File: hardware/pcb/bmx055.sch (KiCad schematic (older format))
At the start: 1 part, among them U3 BMX055

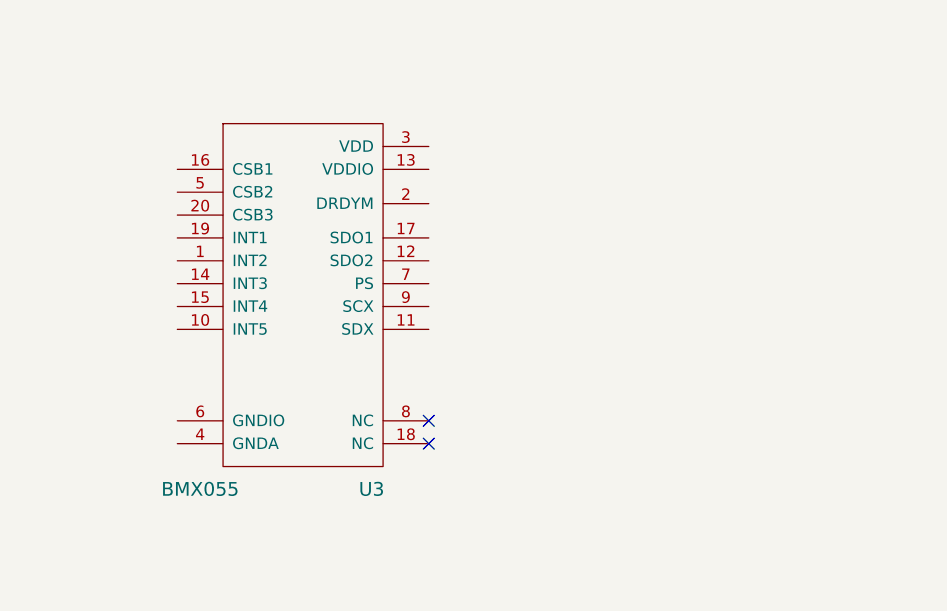
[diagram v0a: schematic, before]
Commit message: Added mcu, connected nrf8001 and flash, new footprint, other changes
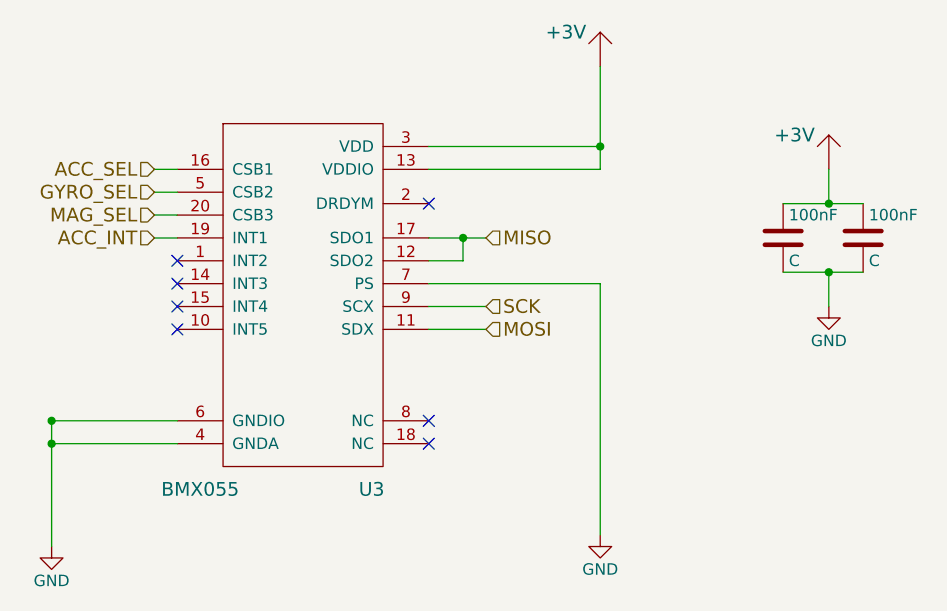
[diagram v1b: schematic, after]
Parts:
- added 100nF (x2): C, symbol C
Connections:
- net MOSI: now reaches U3.11 (SDX)
- net MISO: now reaches U3.12 (SDO2)
- net MISO: now also U3.17 (SDO1)
- net +3V3: now reaches U3.13 (VDDIO)
- net +3V3: now also U3.3 (VDD), 100nF.1, 100nF.1
- net ACC_SEL: now reaches U3.16 (CSB1)
- net ACC_INT: now reaches U3.19 (INT1)
- net MAG_SEL: now reaches U3.20 (CSB3)
- net GND: now reaches U3.4 (GNDA)
- net GND: now also U3.6 (GNDIO), U3.7 (PS), 100nF.2, 100nF.2
- net GYRO_SEL: now reaches U3.5 (CSB2)
- net SCK: now reaches U3.9 (SCX)
- no-connect marks 2 -> 7
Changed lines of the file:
@@
 $Descr A4 11693 8268
 encoding utf-8
-Sheet 4 4
+Sheet 4 5
 Title ""
 Date ""
@@
 NoConn ~ 6150 3650
 NoConn ~ 6150 3550
+$Comp
+L +3V #PWR?
+U 1 1 552EACA4
+P 6900 2000
+F 0 "#PWR?" H 6900 1900 60  0001 C CNN
+F 1 "+3V" H 6750 2150 60  0000 C CNN
+F 2 "" H 6900 2000 60  0000 C CNN
+F 3 "" H 6900 2000 60  0000 C CNN
+	1    6900 2000
+	1    0    0    -1
+$EndComp
+$Comp
+L GND #PWR?
+U 1 1 552EACBF
+P 6900 4050
+F 0 "#PWR?" H 6900 3800 50  0001 C CNN
+F 1 "GND" H 6900 3900 50  0000 C CNN
+F 2 "" H 6900 4050 60  0000 C CNN
+F 3 "" H 6900 4050 60  0000 C CNN
+	1    6900 4050
+	1    0    0    -1
+$EndComp
+$Comp
+L GND #PWR?
+U 1 1 552EACD5
+P 4500 4100
+F 0 "#PWR?" H 4500 3850 50  0001 C CNN
+F 1 "GND" H 4500 3950 50  0000 C CNN
+F 2 "" H 4500 4100 60  0000 C CNN
+F 3 "" H 4500 4100 60  0000 C CNN
+	1    4500 4100
+	1    0    0    -1
+$EndComp
+Wire Wire Line
+	4500 3650 5050 3650
+Wire Wire Line
+	5050 3550 4500 3550
+Connection ~ 4500 3650
+Connection ~ 4500 3550
+Text HLabel 4950 2450 0    60   Input ~ 0
+ACC_SEL
+Text HLabel 4950 2550 0    60   Input ~ 0
+GYRO_SEL
+Text HLabel 4950 2650 0    60   Input ~ 0
+MAG_SEL
+Wire Wire Line
+	4950 2450 5050 2450
+Wire Wire Line
+	5050 2550 4950 2550
+Wire Wire Line
+	4950 2650 5050 2650
+Text HLabel 4950 2750 0    60   Input ~ 0
+ACC_INT
+Wire Wire Line
+	4950 2750 5050 2750
+NoConn ~ 5050 2850
+NoConn ~ 5050 2950
+NoConn ~ 5050 3050
+NoConn ~ 5050 3150
+NoConn ~ 6150 2600
+Text HLabel 6400 2750 2    60   Input ~ 0
+MISO
+Wire Wire Line
+	6150 2750 6400 2750
+Wire Wire Line
+	6150 2850 6300 2850
+Wire Wire Line
+	6300 2850 6300 2750
+Connection ~ 6300 2750
+Text HLabel 6400 3150 2    60   Input ~ 0
+MOSI
+Wire Wire Line
+	6400 3150 6150 3150
+Text HLabel 6400 3050 2    60   Input ~ 0
+SCK
+Wire Wire Line
+	6400 3050 6150 3050
+Wire Wire Line
+	6150 2950 6900 2950
+Wire Wire Line
+	6900 2950 6900 4050
+$Comp
+L +3V #PWR?
+U 1 1 552EBBB1
+P 7900 2450
+F 0 "#PWR?" H 7900 2350 60  0001 C CNN
+F 1 "+3V" H 7750 2600 60  0000 C CNN
+F 2 "" H 7900 2450 60  0000 C CNN
+F 3 "" H 7900 2450 60  0000 C CNN
+	1    7900 2450
+	1    0    0    -1
+$EndComp
+$Comp
+L GND #PWR?
+U 1 1 552EBBC7
+P 7900 3050
+F 0 "#PWR?" H 7900 2800 50  0001 C CNN
+F 1 "GND" H 7900 2900 50  0000 C CNN
+F 2 "" H 7900 3050 60  0000 C CNN
+F 3 "" H 7900 3050 60  0000 C CNN
+	1    7900 3050
+	1    0    0    -1
+$EndComp
+$Comp
+L C 100nF
+U 1 1 552EBBDD
+P 7700 2750
+F 0 "100nF" H 7725 2850 50  0000 L CNN
+F 1 "C" H 7725 2650 50  0000 L CNN
+F 2 "" H 7738 2600 30  0000 C CNN
+F 3 "" H 7700 2750 60  0000 C CNN
+	1    7700 2750
+	1    0    0    -1
+$EndComp
+$Comp
+L C 100nF
+U 1 1 552EBBFD
+P 8050 2750
+F 0 "100nF" H 8075 2850 50  0000 L CNN
+F 1 "C" H 8075 2650 50  0000 L CNN
+F 2 "" H 8088 2600 30  0000 C CNN
+F 3 "" H 8050 2750 60  0000 C CNN
+	1    8050 2750
+	1    0    0    -1
+$EndComp
+Wire Wire Line
+	7700 2900 8050 2900
+Wire Wire Line
+	7900 2900 7900 3050
+Connection ~ 7900 2900
+Wire Wire Line
+	7700 2600 8050 2600
+Wire Wire Line
+	7900 2600 7900 2450
+Connection ~ 7900 2600
+Wire Wire Line
+	4500 3550 4500 4100
+Wire Wire Line
+	6150 2350 6900 2350
+Wire Wire Line
+	6900 2000 6900 2450
+Wire Wire Line
+	6900 2450 6150 2450
+Connection ~ 6900 2350
 $EndSCHEMATC
